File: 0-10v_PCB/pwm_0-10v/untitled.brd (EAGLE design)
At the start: 38.1 x 22.5 mm, 13 parts, among them U1 OP07CDR, U2 OP07CDR, U3 OP07CDR

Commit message: made centroid file
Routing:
- net +12V: track 0.00 -> 41.2 mm, vias 0 -> 4
- net GND: track 0.00 -> 3.21 mm, vias 0 -> 2
- added copper zone on layer 1, net GND
- added copper zone on layer 16, net GND
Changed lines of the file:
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@@
 <elements>
 <element name="C1" library="rcl" library_urn="urn:adsk.eagle:library:334" package="C0805" package3d_urn="urn:adsk.eagle:package:23617/2" value="10uF" x="12.065" y="20.955" smashed="yes" rot="R90">
-<attribute name="NAME" x="10.795" y="19.685" size="1.27" layer="25" rot="R90"/>
 <attribute name="POPULARITY" value="88" x="33.655" y="37.465" size="1.778" layer="27" rot="R90" display="off"/>
 <attribute name="SPICEPREFIX" value="C" x="33.655" y="37.465" size="1.778" layer="27" rot="R90" display="off"/>
@@
 </element>
 <element name="R1" library="rcl" library_urn="urn:adsk.eagle:library:334" package="M0805" package3d_urn="urn:adsk.eagle:package:23556/2" value="10k" x="6.985" y="20.955" smashed="yes" rot="R270">
-<attribute name="NAME" x="8.255" y="22.225" size="1.27" layer="25" rot="R270"/>
 <attribute name="POPULARITY" value="45" x="-14.605" y="-0.635" size="1.778" layer="27" rot="R270" display="off"/>
 <attribute name="SPICEPREFIX" value="R" x="-14.605" y="-0.635" size="1.778" layer="27" rot="R270" display="off"/>
-<attribute name="VALUE" x="4.445" y="22.225" size="1.27" layer="27" rot="R270"/>
+<attribute name="VALUE" x="8.255" y="22.225" size="1.27" layer="27" rot="R270"/>
 </element>
 <element name="SL1" library="con-amp-quick" library_urn="urn:adsk.eagle:library:125" package="02P" package3d_urn="urn:adsk.eagle:package:5956/1" value="" x="9.525" y="28.575" smashed="yes" rot="R180">
 <attribute name="MF" value="" x="-5.715" y="41.275" size="1.778" layer="27" rot="R180" display="off"/>
 <attribute name="MPN" value="" x="-5.715" y="41.275" size="1.778" layer="27" rot="R180" display="off"/>
-<attribute name="NAME" x="11.811" y="25.6286" size="1.27" layer="25" ratio="10" rot="R180"/>
 <attribute name="OC_FARNELL" value="unknown" x="-5.715" y="41.275" size="1.778" layer="27" rot="R180" display="off"/>
 <attribute name="OC_NEWARK" value="unknown" x="-5.715" y="41.275" size="1.778" layer="27" rot="R180" display="off"/>
@@
 <attribute name="MF" value="" x="30.48" y="41.275" size="1.778" layer="27" rot="R90" display="off"/>
 <attribute name="MPN" value="" x="30.48" y="41.275" size="1.778" layer="27" rot="R90" display="off"/>
-<attribute name="NAME" x="14.8336" y="17.399" size="1.27" layer="25" ratio="10" rot="R90"/>
 <attribute name="OC_FARNELL" value="unknown" x="30.48" y="41.275" size="1.778" layer="27" rot="R90" display="off"/>
 <attribute name="OC_NEWARK" value="unknown" x="30.48" y="41.275" size="1.778" layer="27" rot="R90" display="off"/>
@@
 </element>
 <element name="C2" library="rcl" library_urn="urn:adsk.eagle:library:334" package="C0805" package3d_urn="urn:adsk.eagle:package:23617/2" value="10uF" x="3.175" y="20.955" smashed="yes" rot="R90">
-<attribute name="NAME" x="1.905" y="19.685" size="1.27" layer="25" rot="R90"/>
 <attribute name="POPULARITY" value="88" x="24.765" y="37.465" size="1.778" layer="27" rot="R90" display="off"/>
 <attribute name="SPICEPREFIX" value="C" x="24.765" y="37.465" size="1.778" layer="27" rot="R90" display="off"/>
-<attribute name="VALUE" x="5.715" y="19.685" size="1.27" layer="27" rot="R90"/>
+<attribute name="VALUE" x="1.905" y="19.05" size="1.27" layer="27" rot="R90"/>
 </element>
 <element name="R2" library="rcl" library_urn="urn:adsk.eagle:library:334" package="M0805" package3d_urn="urn:adsk.eagle:package:23556/2" value="10k" x="-1.905" y="20.955" smashed="yes" rot="R270">
-<attribute name="NAME" x="-0.635" y="22.225" size="1.27" layer="25" rot="R270"/>
 <attribute name="POPULARITY" value="45" x="-23.495" y="-0.635" size="1.778" layer="27" rot="R270" display="off"/>
 <attribute name="SPICEPREFIX" value="R" x="-23.495" y="-0.635" size="1.778" layer="27" rot="R270" display="off"/>
@@
 <attribute name="MF" value="" x="-14.605" y="41.275" size="1.778" layer="27" rot="R180" display="off"/>
 <attribute name="MPN" value="" x="-14.605" y="41.275" size="1.778" layer="27" rot="R180" display="off"/>
-<attribute name="NAME" x="2.921" y="25.6286" size="1.27" layer="25" ratio="10" rot="R180"/>
 <attribute name="OC_FARNELL" value="unknown" x="-14.605" y="41.275" size="1.778" layer="27" rot="R180" display="off"/>
 <attribute name="OC_NEWARK" value="unknown" x="-14.605" y="41.275" size="1.778" layer="27" rot="R180" display="off"/>
@@
 </element>
 <element name="C3" library="rcl" library_urn="urn:adsk.eagle:library:334" package="C0805" package3d_urn="urn:adsk.eagle:package:23617/2" value="10uF" x="-5.715" y="20.955" smashed="yes" rot="R90">
-<attribute name="NAME" x="-6.985" y="19.685" size="1.27" layer="25" rot="R90"/>
 <attribute name="POPULARITY" value="88" x="15.875" y="37.465" size="1.778" layer="27" rot="R90" display="off"/>
 <attribute name="SPICEPREFIX" value="C" x="15.875" y="37.465" size="1.778" layer="27" rot="R90" display="off"/>
-<attribute name="VALUE" x="-3.175" y="19.685" size="1.27" layer="27" rot="R90"/>
+<attribute name="VALUE" x="-6.985" y="19.05" size="1.27" layer="27" rot="R90"/>
 </element>
 <element name="R3" library="rcl" library_urn="urn:adsk.eagle:library:334" package="M0805" package3d_urn="urn:adsk.eagle:package:23556/2" value="10k" x="-10.795" y="20.955" smashed="yes" rot="R270">
-<attribute name="NAME" x="-9.525" y="22.225" size="1.27" layer="25" rot="R270"/>
 <attribute name="POPULARITY" value="45" x="-32.385" y="-0.635" size="1.778" layer="27" rot="R270" display="off"/>
 <attribute name="SPICEPREFIX" value="R" x="-32.385" y="-0.635" size="1.778" layer="27" rot="R270" display="off"/>
@@
 <attribute name="MF" value="" x="-23.495" y="41.275" size="1.778" layer="27" rot="R180" display="off"/>
 <attribute name="MPN" value="" x="-23.495" y="41.275" size="1.778" layer="27" rot="R180" display="off"/>
-<attribute name="NAME" x="-5.969" y="25.6286" size="1.27" layer="25" ratio="10" rot="R180"/>
 <attribute name="OC_FARNELL" value="unknown" x="-23.495" y="41.275" size="1.778" layer="27" rot="R180" display="off"/>
 <attribute name="OC_NEWARK" value="unknown" x="-23.495" y="41.275" size="1.778" layer="27" rot="R180" display="off"/>
@@
 <contactref element="U2" pad="4"/>
 <contactref element="C2" pad="2"/>
-<wire x1="12.065" y1="21.905" x2="17.78" y2="20.955" width="0" layer="19" extent="1-1"/>
-<wire x1="3.175" y1="21.905" x2="12.065" y2="21.905" width="0" layer="19" extent="1-1"/>
-<wire x1="-5.715" y1="21.905" x2="3.175" y2="21.905" width="0" layer="19" extent="1-1"/>
-<wire x1="7.055" y1="11.43" x2="3.175" y2="21.905" width="0" layer="19" extent="1-1"/>
-<wire x1="-1.835" y1="11.43" x2="7.055" y2="11.43" width="0" layer="19" extent="1-1"/>
-<wire x1="-10.725" y1="11.43" x2="-1.835" y2="11.43" width="0" layer="19" extent="1-1"/>
+<polygon width="0.1524" layer="1">
+<vertex x="-17.78" y="31.75"/>
+<vertex x="-17.78" y="8.255"/>
+<vertex x="20.32" y="8.255"/>
+<vertex x="20.32" y="31.75"/>
+</polygon>
+<polygon width="0.1524" layer="16">
+<vertex x="-17.78" y="31.75"/>
+<vertex x="-17.78" y="8.255"/>
+<vertex x="20.32" y="8.255"/>
+<vertex x="20.32" y="31.75"/>
+</polygon>
+<wire x1="-10.725" y1="11.43" x2="-10.16" y2="10.865" width="0.1524" layer="1"/>
+<wire x1="-10.16" y1="10.865" x2="-10.16" y2="10.2842" width="0.1524" layer="1"/>
+<wire x1="-10.16" y1="10.2842" x2="-10.16" y2="10.16" width="0.1524" layer="1"/>
+<via x="-10.16" y="10.2842" extent="1-16" drill="0.35"/>
+<wire x1="-10.16" y1="10.2842" x2="-10.16" y2="10.16" width="0.1524" layer="16"/>
+<wire x1="-1.835" y1="11.43" x2="-0.254" y2="11.43" width="0.1524" layer="1"/>
+<via x="-0.254" y="11.43" extent="1-16" drill="0.35"/>
 </signal>
 <signal name="+12V">
@@
 <contactref element="U3" pad="7"/>
 <contactref element="U2" pad="7"/>
-<wire x1="11.995" y1="13.97" x2="17.78" y2="18.415" width="0" layer="19" extent="1-1"/>
-<wire x1="3.105" y1="13.97" x2="11.995" y2="13.97" width="0" layer="19" extent="1-1"/>
-<wire x1="-5.785" y1="13.97" x2="3.105" y2="13.97" width="0" layer="19" extent="1-1"/>
+<wire x1="17.78" y1="18.415" x2="13.335" y2="13.97" width="0.1524" layer="1"/>
+<wire x1="13.335" y1="13.97" x2="11.995" y2="13.97" width="0.1524" layer="1"/>
+<wire x1="11.995" y1="13.97" x2="10.795" y2="13.97" width="0.1524" layer="1"/>
+<wire x1="10.795" y1="13.97" x2="10.16" y2="13.335" width="0.1524" layer="1"/>
+<wire x1="10.16" y1="13.335" x2="10.16" y2="12.065" width="0.1524" layer="1"/>
+<wire x1="10.16" y1="12.065" x2="9.525" y2="11.43" width="0.1524" layer="1"/>
+<via x="9.525" y="11.43" extent="1-16" drill="0.35"/>
+<wire x1="9.525" y1="11.43" x2="9.525" y2="10.795" width="0.1524" layer="16"/>
+<wire x1="9.525" y1="10.795" x2="8.89" y2="10.16" width="0.1524" layer="16"/>
+<wire x1="8.89" y1="10.16" x2="1.27" y2="10.16" width="0.1524" layer="16"/>
+<wire x1="1.27" y1="10.16" x2="0.635" y2="10.795" width="0.1524" layer="16"/>
+<via x="0.635" y="10.795" extent="1-16" drill="0.35"/>
+<via x="0.635" y="10.795" extent="1-16" drill="0.35"/>
+<wire x1="0.635" y1="10.795" x2="0" y2="10.16" width="0.1524" layer="16"/>
+<wire x1="0" y1="10.16" x2="-7.62" y2="10.16" width="0.1524" layer="16"/>
+<wire x1="-7.62" y1="10.16" x2="-8.255" y2="10.795" width="0.1524" layer="16"/>
+<via x="-8.255" y="10.795" extent="1-16" drill="0.35"/>
+<wire x1="-8.255" y1="12.7" x2="-6.985" y2="13.97" width="0.1524" layer="1"/>
+<wire x1="-6.985" y1="13.97" x2="-5.785" y2="13.97" width="0.1524" layer="1"/>
+<wire x1="-8.255" y1="10.795" x2="-8.255" y2="12.7" width="0.1524" layer="1"/>
+<wire x1="0.635" y1="12.7" x2="1.905" y2="13.97" width="0.1524" layer="1"/>
+<wire x1="1.905" y1="13.97" x2="3.105" y2="13.97" width="0.1524" layer="1"/>
+<wire x1="0.635" y1="10.795" x2="0.635" y2="12.7" width="0.1524" layer="1"/>
 </signal>
 <signal name="N$1">

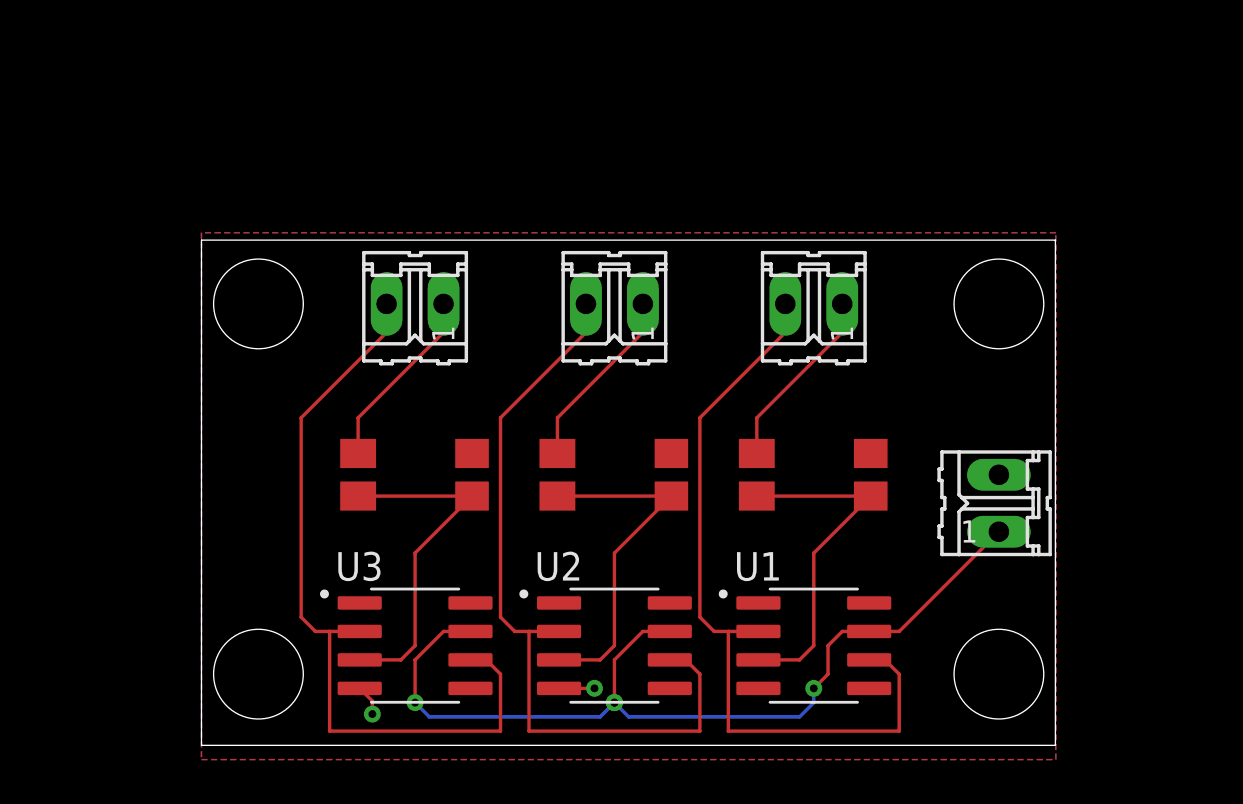
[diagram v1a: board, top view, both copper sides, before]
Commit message: changed screw terminals to correct size
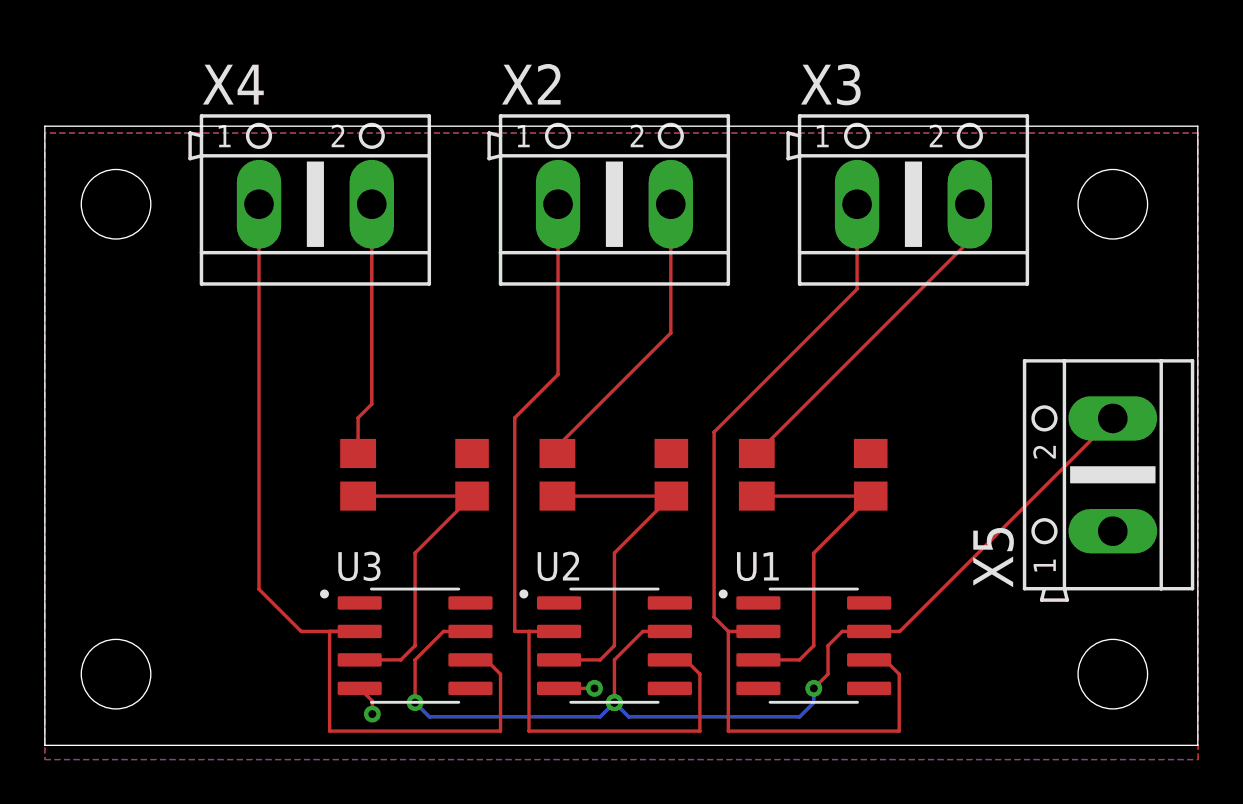
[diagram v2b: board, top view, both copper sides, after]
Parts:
- removed SL1, SL2, SL3, SL4: (no value), con-amp-quick:02P
- added X2, X3, X4, X5: (no value), con-ptr500:AK500/2
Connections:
- net +12V: now also X5.2; no longer SL2.1
- net GND: now also X5.1; no longer SL2.2
- net N$1: now also X3.2; no longer SL1.1
- net N$3: now also X2.2; no longer SL3.1
- net N$5: now also X4.2; no longer SL4.1
- net OUT_A: now also X3.1; no longer SL1.2
- net OUT_A1: now also X2.1; no longer SL3.2
- net OUT_A2: now also X4.1; no longer SL4.2
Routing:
- net +12V: track 41.2 -> 48.3 mm
- net N$1: track 8.25 -> 15.0 mm
- net OUT_A2: track 34.6 -> 40.0 mm
- net N$3: track 8.25 -> 13.2 mm
- net OUT_A: track 34.6 -> 39.5 mm
- net OUT_A1: track 34.6 -> 38.0 mm
- net N$5: track 8.25 -> 11.4 mm
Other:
- board size 38.1 x 22.5 mm -> 51.4 x 27.6 mm
